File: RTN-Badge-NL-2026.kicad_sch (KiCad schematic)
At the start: 21 parts, among them J1 USB_A_Edge_Connector, J2 DEBUG, J3 GPIO, SW1 BOOT, SW2 RST, SW3 USER1, SW4 USER2, U1 CH32V203F6P6, U2 ME6211C33M5, Y1 8MHz

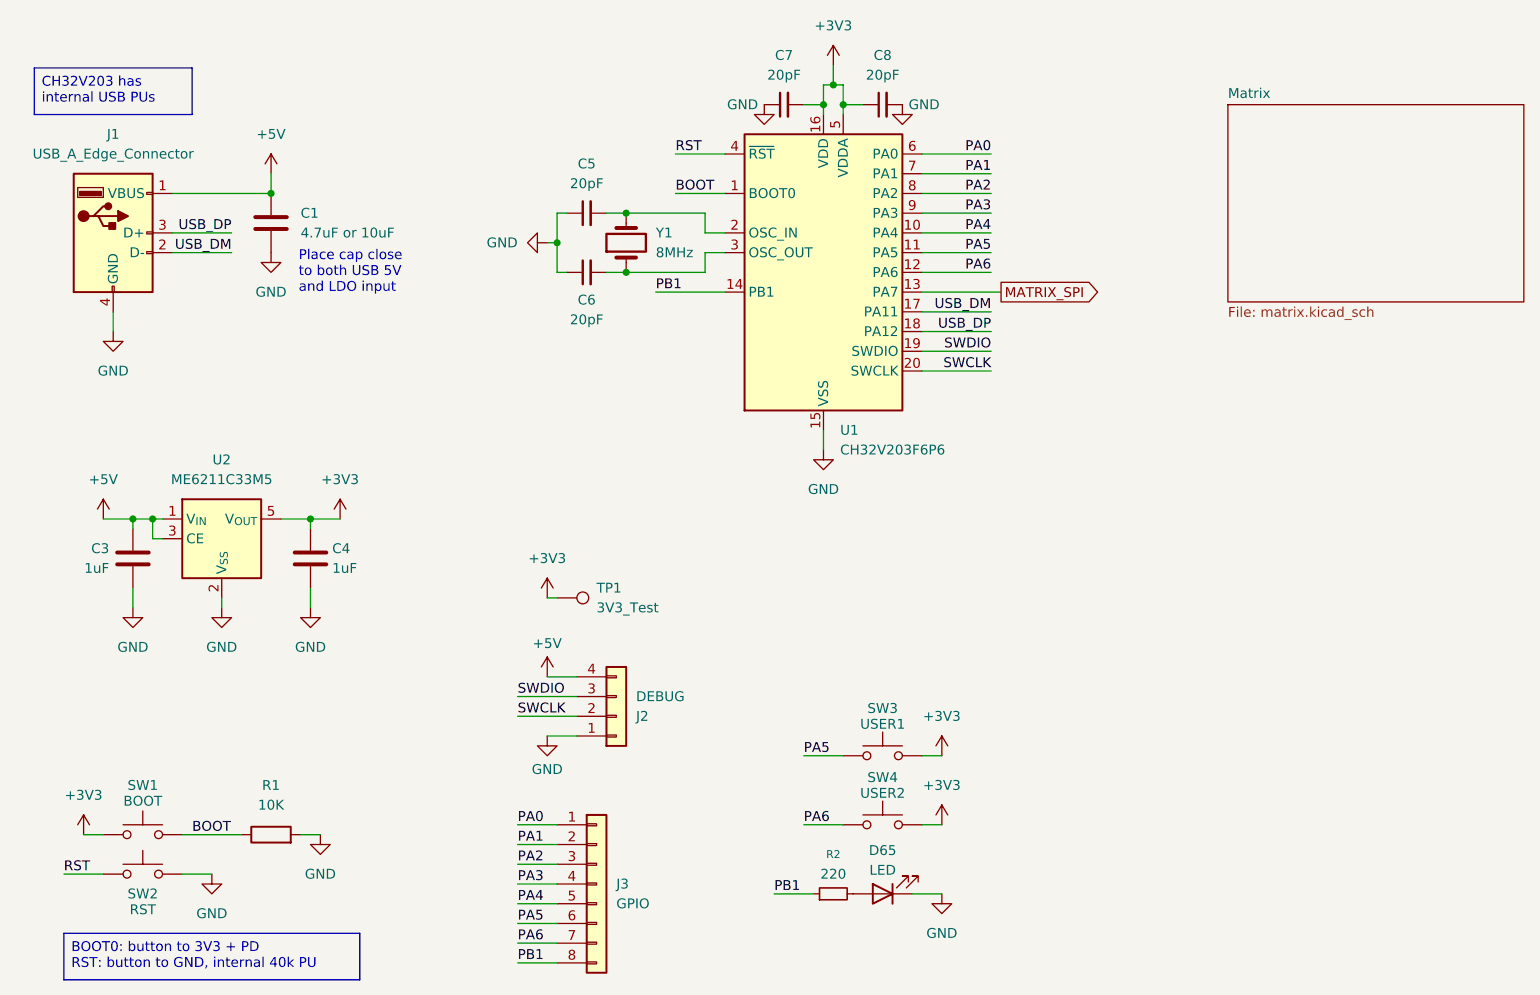
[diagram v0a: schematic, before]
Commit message: Adjust PCB to use components available in JLCPCB's product library
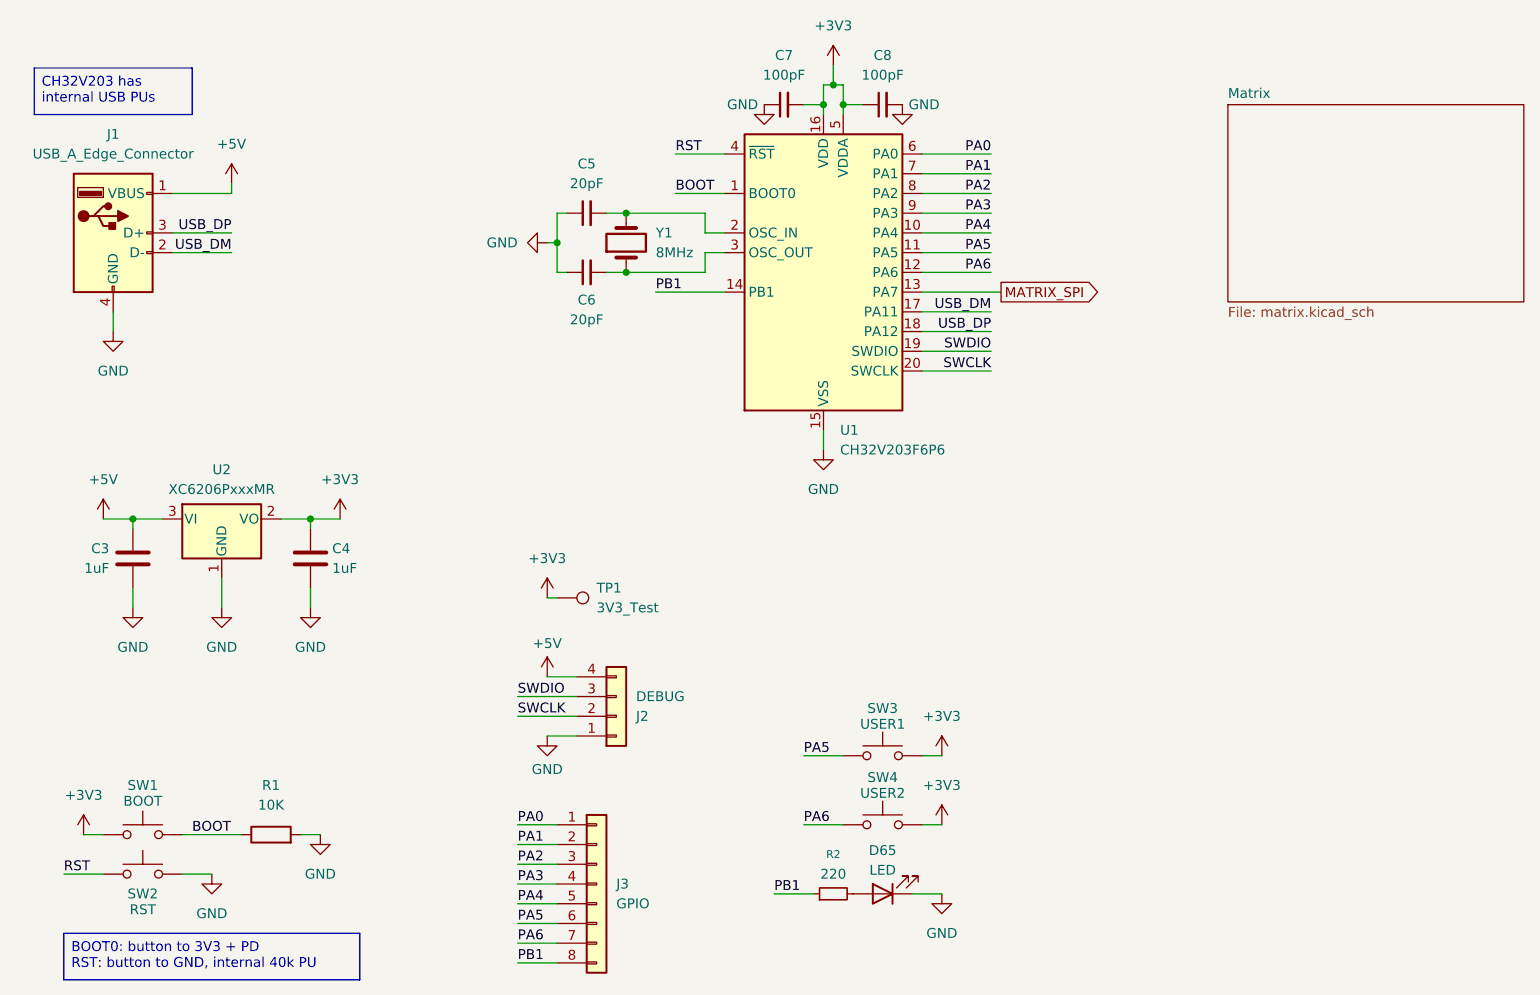
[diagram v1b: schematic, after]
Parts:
- removed C1: 4.7uF or 10uF, Capacitor_SMD:C_0603_1608Metric, symbol Device:C
- removed U2: ME6211C33M5, Package_TO_SOT_SMD:SOT-23-5, symbol Regulator_Linear:ME6211C33M5
- added U2: XC6206PxxxMR, Package_TO_SOT_SMD:SOT-23-3, symbol Regulator_Linear:XC6206PxxxMR
- C7, C8: value 20pF -> 100pF
- SW1, SW2, SW3, SW4: footprint Button_Switch_SMD:SW_Push_1P1T_NO_CK_KMR2 -> Button_Switch_SMD:SW_SPST_TS-1088-xR020
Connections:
- net +3V3: now also U2.2 (VO)
- net +5V: now also U2.3 (VI)
- net GND: now also U2.1 (GND)
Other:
- note removed: "Place cap close to both USB 5V and LDO input"
